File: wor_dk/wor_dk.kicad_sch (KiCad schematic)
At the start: 13 parts, among them J101 Conn_01x02, J102 Conn_02x03_Odd_Even, J103 Conn_02x03_Odd_Even, J104 Conn_01x02

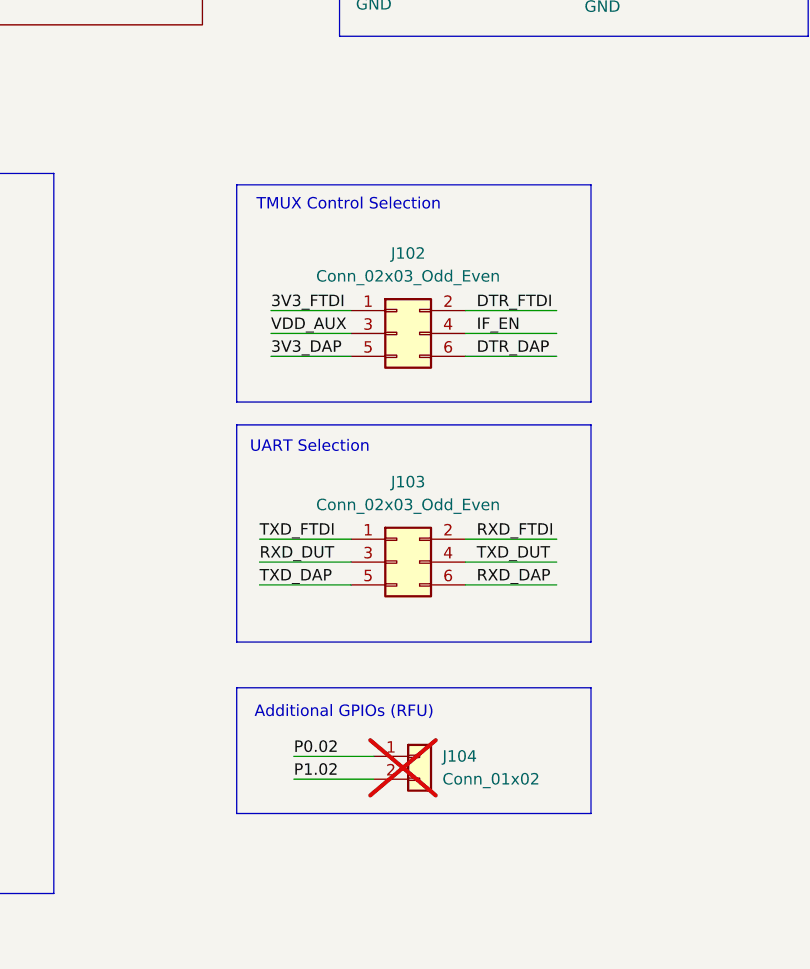
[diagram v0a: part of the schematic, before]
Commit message: wor_dk: add GND pin headers
This is just for convenience.
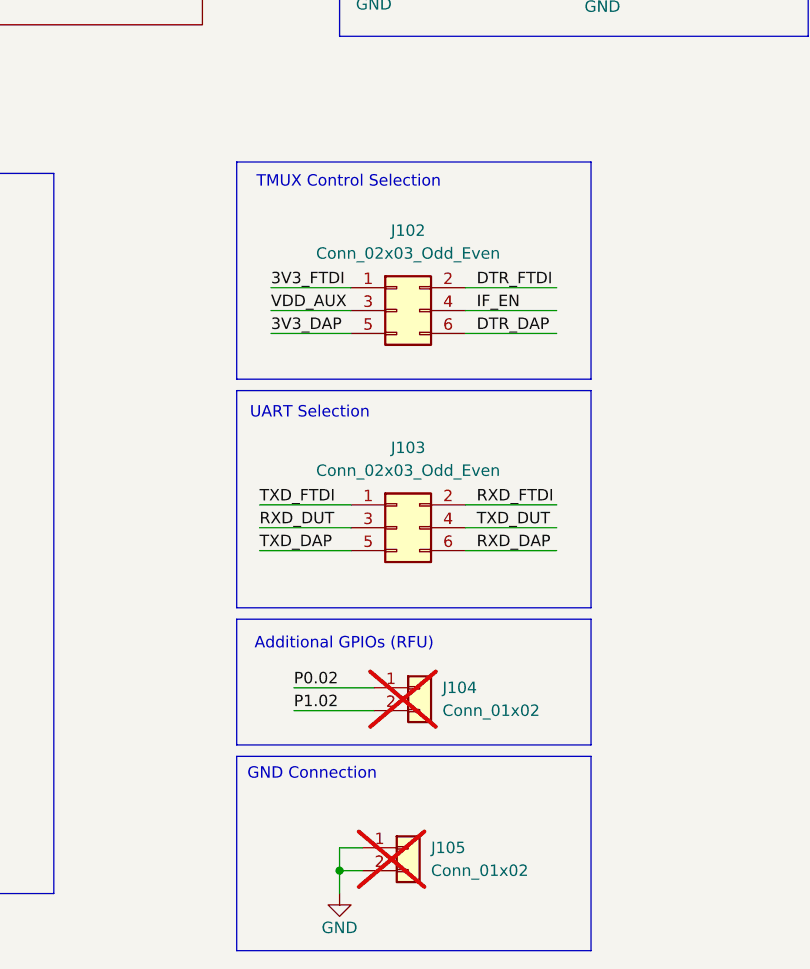
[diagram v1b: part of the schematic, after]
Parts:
- added J105: Conn_01x02, Connector_PinHeader_2.54mm:PinHeader_1x02_P2.54mm_Vertical, symbol Connector_Generic:Conn_01x02
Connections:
- net GND: now also J105.1 (Pin_1), J105.2 (Pin_2)
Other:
- note added: "GND Connection"
- moved on the sheet: J102, J103, J104
